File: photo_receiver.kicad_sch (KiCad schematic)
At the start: 7 parts, among them J5 Receiver Connector

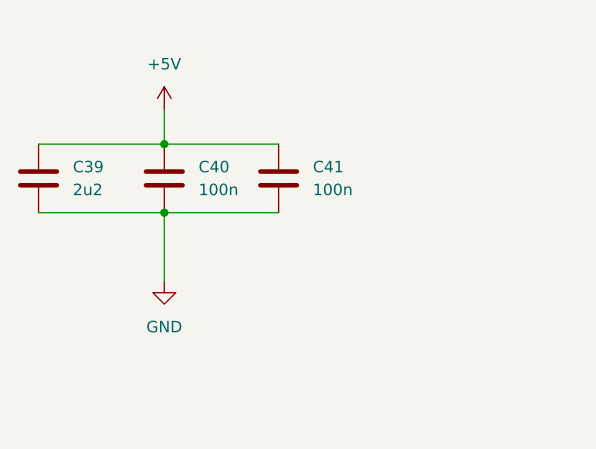
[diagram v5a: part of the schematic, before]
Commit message: Place and route optic side parts
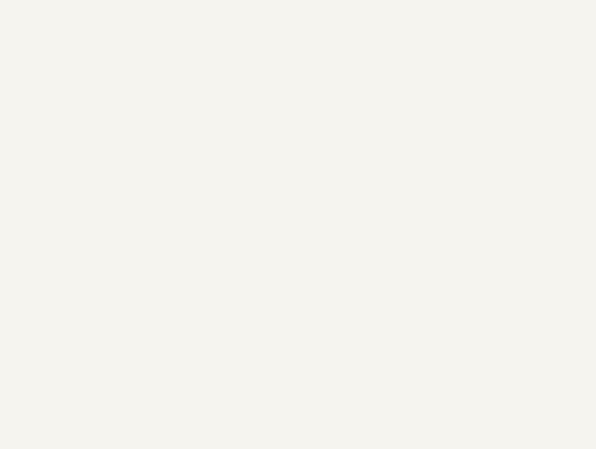
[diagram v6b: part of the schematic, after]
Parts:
- removed C39: 2u2, Capacitor_Tantalum_SMD:CP_EIA-3528-15_AVX-H_Pad1.50x2.35mm_HandSolder, symbol Device:C
- removed C40, C41: 100n, Capacitor_SMD:C_0805_2012Metric_Pad1.18x1.45mm_HandSolder, symbol Device:C
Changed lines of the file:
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@@
 (kicad_sch (version 20211123) (generator eeschema)
   (paper "A4")
-  (junction (at 52.07 87.63) (diameter 0) (color 0 0 0 0)
-  )
   (junction (at 132.08 113.03) (diameter 0) (color 0 0 0 0)
-  )
-  (junction (at 52.07 95.25) (diameter 0) (color 0 0 0 0)
   )
   (junction (at 142.24 97.79) (diameter 0) (color 0 0 0 0)
@@
     (stroke (width 0) (type default) (color 0 0 0 0))
   )
-  (wire (pts (xy 52.07 83.82) (xy 52.07 87.63))
-    (stroke (width 0) (type default) (color 0 0 0 0))
-  )
   (wire (pts (xy 142.24 97.79) (xy 142.24 104.14))
     (stroke (width 0) (type default) (color 0 0 0 0))
@@
   )
   (wire (pts (xy 142.24 113.03) (xy 132.08 113.03))
-    (stroke (width 0) (type default) (color 0 0 0 0))
-  )
-  (wire (pts (xy 52.07 87.63) (xy 64.77 87.63))
     (stroke (width 0) (type default) (color 0 0 0 0))
   )
@@
     (stroke (width 0) (type default) (color 0 0 0 0))
   )
-  (wire (pts (xy 38.1 87.63) (xy 52.07 87.63))
-    (stroke (width 0) (type default) (color 0 0 0 0))
-  )
   (wire (pts (xy 143.51 91.44) (xy 146.05 91.44))
-    (stroke (width 0) (type default) (color 0 0 0 0))
-  )
-  (wire (pts (xy 52.07 95.25) (xy 52.07 102.87))
     (stroke (width 0) (type default) (color 0 0 0 0))
   )
@@
   )
   (wire (pts (xy 114.3 91.44) (xy 114.3 88.9))
-    (stroke (width 0) (type default) (color 0 0 0 0))
-  )
-  (wire (pts (xy 38.1 95.25) (xy 52.07 95.25))
-    (stroke (width 0) (type default) (color 0 0 0 0))
-  )
-  (wire (pts (xy 52.07 95.25) (xy 64.77 95.25))
     (stroke (width 0) (type default) (color 0 0 0 0))
   )
@@
     )
     (property "Source" "L3 store" (id 4) (at 142.24 107.95 0)
-      (effects (font (size 1.27 1.27)) hide)
-    )
-    (pin "1")
-    (pin "2")
-  )
-  (symbol (lib_id "Device:C") (at 64.77 91.44 0) (unit 1)
-    (in_bom yes) (on_board yes) (fields_autoplaced)
-    (property "Reference" "C41" (id 0) (at 68.58 90.1699 0)
-      (effects (font (size 1.27 1.27)) (justify left))
-    )
-    (property "Value" "100n" (id 1) (at 68.58 92.7099 0)
-      (effects (font (size 1.27 1.27)) (justify left))
-    )
-    (property "Footprint" "Capacitor_SMD:C_0805_2012Metric_Pad1.18x1.45mm_HandSolder" (id 2) (at 65.7352 95.25 0)
-      (effects (font (size 1.27 1.27)) hide)
-    )
-    (property "Datasheet" "~" (id 3) (at 64.77 91.44 0)
-      (effects (font (size 1.27 1.27)) hide)
-    )
-    (property "Source" "L3 store" (id 4) (at 64.77 91.44 0)
       (effects (font (size 1.27 1.27)) hide)
     )
@@
     (pin "1")
   )
-  (symbol (lib_id "Device:C") (at 52.07 91.44 0) (unit 1)
-    (in_bom yes) (on_board yes) (fields_autoplaced)
-    (property "Reference" "C40" (id 0) (at 55.88 90.1699 0)
-      (effects (font (size 1.27 1.27)) (justify left))
-    )
-    (property "Value" "100n" (id 1) (at 55.88 92.7099 0)
-      (effects (font (size 1.27 1.27)) (justify left))
-    )
-    (property "Footprint" "Capacitor_SMD:C_0805_2012Metric_Pad1.18x1.45mm_HandSolder" (id 2) (at 53.0352 95.25 0)
-      (effects (font (size 1.27 1.27)) hide)
-    )
-    (property "Datasheet" "~" (id 3) (at 52.07 91.44 0)
-      (effects (font (size 1.27 1.27)) hide)
-    )
-    (property "Source" "L3 store" (id 4) (at 52.07 91.44 0)
-      (effects (font (size 1.27 1.27)) hide)
-    )
-    (pin "1")
-    (pin "2")
-  )
-  (symbol (lib_id "power:+5V") (at 52.07 83.82 0) (unit 1)
-    (in_bom yes) (on_board yes) (fields_autoplaced)
-    (property "Reference" "#PWR0106" (id 0) (at 52.07 87.63 0)
-      (effects (font (size 1.27 1.27)) hide)
-    )
-    (property "Value" "+5V" (id 1) (at 52.07 78.74 0))
-    (property "Footprint" "" (id 2) (at 52.07 83.82 0)
-      (effects (font (size 1.27 1.27)) hide)
-    )
-    (property "Datasheet" "" (id 3) (at 52.07 83.82 0)
-      (effects (font (size 1.27 1.27)) hide)
-    )
-    (pin "1")
-  )
-  (symbol (lib_id "power:GND") (at 52.07 102.87 0) (unit 1)
-    (in_bom yes) (on_board yes) (fields_autoplaced)
-    (property "Reference" "#PWR053" (id 0) (at 52.07 109.22 0)
-      (effects (font (size 1.27 1.27)) hide)
-    )
-    (property "Value" "GND" (id 1) (at 52.07 107.95 0))
-    (property "Footprint" "" (id 2) (at 52.07 102.87 0)
-      (effects (font (size 1.27 1.27)) hide)
-    )
-    (property "Datasheet" "" (id 3) (at 52.07 102.87 0)
-      (effects (font (size 1.27 1.27)) hide)
-    )
-    (pin "1")
-  )
-  (symbol (lib_id "Device:C") (at 38.1 91.44 0) (unit 1)
-    (in_bom yes) (on_board yes) (fields_autoplaced)
-    (property "Reference" "C39" (id 0) (at 41.91 90.1699 0)
-      (effects (font (size 1.27 1.27)) (justify left))
-    )
-    (property "Value" "2u2" (id 1) (at 41.91 92.7099 0)
-      (effects (font (size 1.27 1.27)) (justify left))
-    )
-    (property "Footprint" "Capacitor_Tantalum_SMD:CP_EIA-3528-15_AVX-H_Pad1.50x2.35mm_HandSolder" (id 2) (at 39.0652 95.25 0)
-      (effects (font (size 1.27 1.27)) hide)
-    )
-    (property "Datasheet" "~" (id 3) (at 38.1 91.44 0)
-      (effects (font (size 1.27 1.27)) hide)
-    )
-    (property "Source" "L3 store" (id 4) (at 38.1 91.44 0)
-      (effects (font (size 1.27 1.27)) hide)
-    )
-    (pin "1")
-    (pin "2")
-  )
 )

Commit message: tweaked power circuit, sorted drc errors and warnings, visual checked pcb
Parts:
- J5: footprint CONN_73391-0070_MOL -> SMA Connector:733910070
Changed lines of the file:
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@@
       (effects (font (size 1.27 1.27)) (justify left))
     )
-    (property "Footprint" "CONN_73391-0070_MOL" (id 2) (at 142.494 81.28 0)
+    (property "Footprint" "SMA Connector:733910070" (id 2) (at 142.494 81.28 0)
       (effects (font (size 1.524 1.524)) hide)
     )
